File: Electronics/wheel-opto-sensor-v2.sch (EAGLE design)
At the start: 9 parts

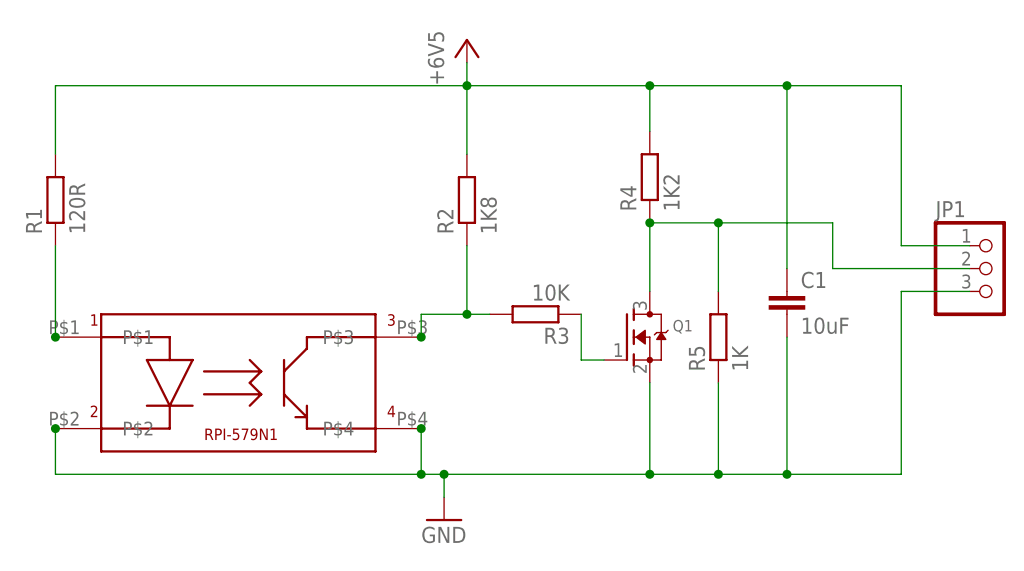
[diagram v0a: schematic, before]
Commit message: Added LED to shield, and anti-short safety diode to the charge circuit.
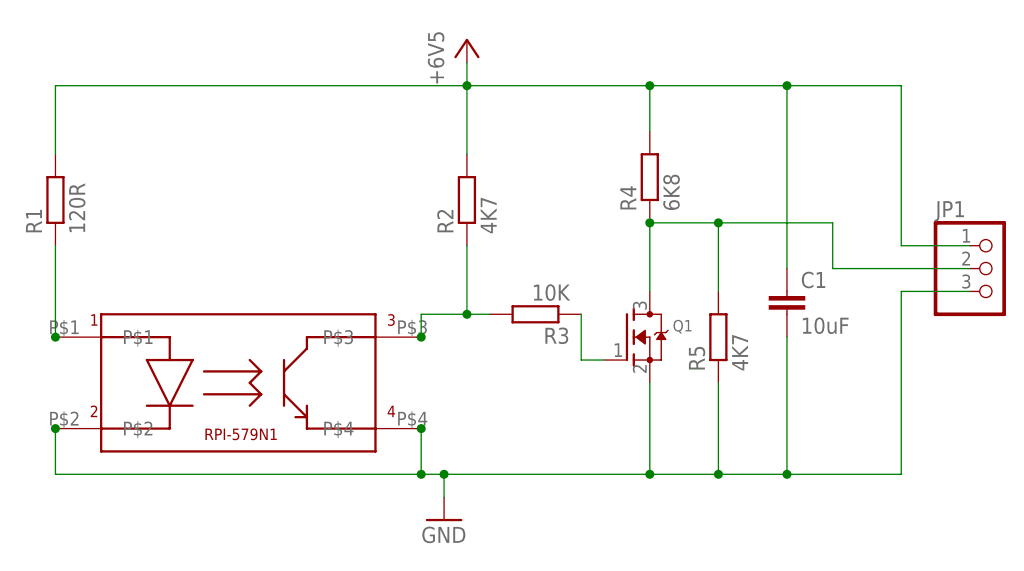
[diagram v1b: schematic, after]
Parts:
- R2: value 1K8 -> 4K7
- R4: value 1K2 -> 6K8
- R5: value 1K -> 4K7
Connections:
- net +3V3 renamed +6V5
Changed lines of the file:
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@@
 <?xml version="1.0" encoding="utf-8"?>
 <!DOCTYPE eagle SYSTEM "eagle.dtd">
-<eagle version="7.5.0">
+<eagle version="8.2.1">
 <drawing>
 <settings>
@@
 <part name="+3V1" library="supply1" deviceset="+3V3" device="" value="+6V5"/>
 <part name="R1" library="rcl" deviceset="R-EU_" device="M0805" value="120R"/>
-<part name="R2" library="rcl" deviceset="R-EU_" device="M0805" value="1K8"/>
+<part name="R2" library="rcl" deviceset="R-EU_" device="M0805" value="4K7"/>
 <part name="R3" library="rcl" deviceset="R-EU_" device="M0805" value="10K"/>
-<part name="R4" library="rcl" deviceset="R-EU_" device="M0805" value="1K2"/>
+<part name="R4" library="rcl" deviceset="R-EU_" device="M0805" value="6K8"/>
 <part name="C1" library="rcl" deviceset="C-EU" device="C1206" value="10uF"/>
 <part name="JP1" library="pinhead" deviceset="PINHD-1X3" device=""/>
-<part name="R5" library="rcl" deviceset="R-EU_" device="M0805" value="1K"/>
+<part name="R5" library="rcl" deviceset="R-EU_" device="M0805" value="4K7"/>
 <part name="U$1" library="reprapltd" deviceset="RPI-579N1" device=""/>
 </parts>
@@
 </segment>
 </net>
-<net name="+3V3" class="0">
+<net name="+6V5" class="0">
 <segment>
 <pinref part="R2" gate="G$1" pin="2"/>
